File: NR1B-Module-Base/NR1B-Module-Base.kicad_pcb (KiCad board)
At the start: 2 copper layers, 70.5 x 134 mm, 3 parts, among them J1 Conn_02x04_Odd_Even, J2 Conn_02x04_Odd_Even, X1 NUCLEO144-ZIO

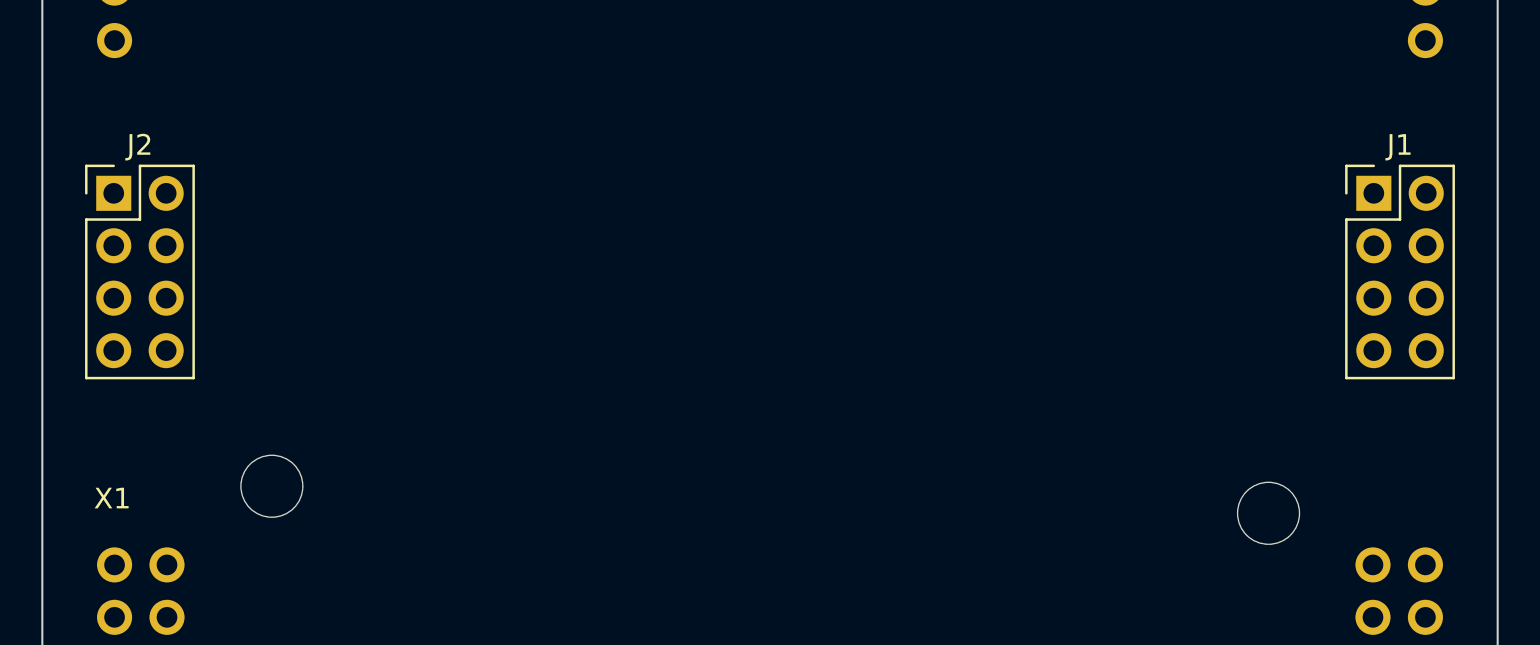
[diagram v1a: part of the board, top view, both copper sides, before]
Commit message: Updated template to match new interconnect spec
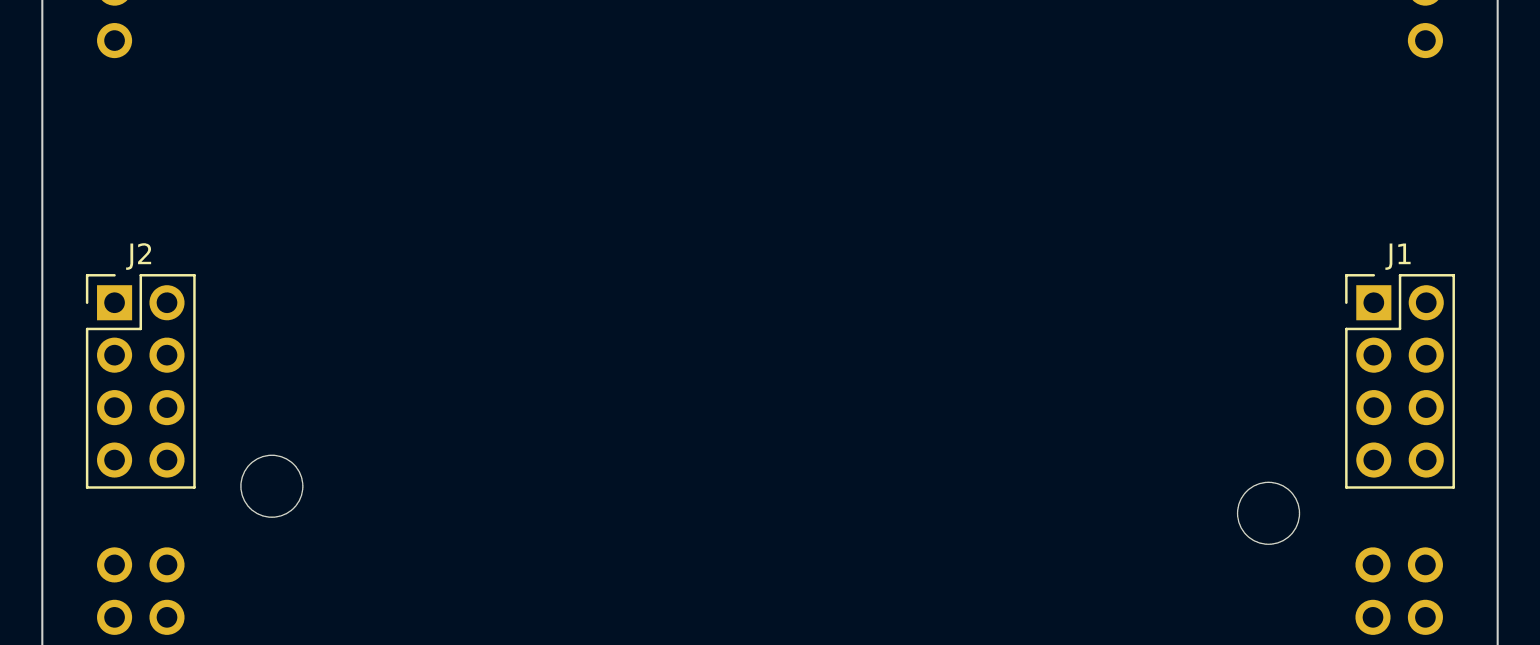
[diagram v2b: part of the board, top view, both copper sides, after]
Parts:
- moved J2 5.30 mm to (163.0, 99.3)
- moved J1 5.30 mm to (224.0, 99.3)
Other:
- board text added: "X1A"
- board text added: "X2A"
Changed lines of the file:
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@@
   (net 160 "unconnected-(J2-Pad8)")
   (footprint "Connector_PinHeader_2.54mm:PinHeader_2x04_P2.54mm_Vertical" (layer "F.Cu")
-    (at 162.96 94)
+    (at 163 99.3)
     (descr "Through hole straight pin header, 2x04, 2.54mm pitch, double rows")
     (tags "Through hole pin header THT 2x04 2.54mm double row")
@@
     (property "Sheetname" "")
     (attr through_hole)
-    (fp_text reference "X1" (at -0.1 -3.2) (layer "F.SilkS")
+    (fp_text reference "X1" (at -0.1 -3.2) (layer "F.SilkS") hide
       (effects (font (size 1 1) (thickness 0.15)))
     )
@@
       (effects (font (size 1 1) (thickness 0.15)))
     )
-    (fp_line (start 41.25 -32.24) (end 50.25 -32.24) (layer "F.CrtYd") (width 0.05))
-    (fp_line (start 67.25 102.16) (end 48.65 102.16) (layer "F.CrtYd") (width 0.05))
-    (fp_line (start 67.25 102.16) (end 67.25 -32.24) (layer "F.CrtYd") (width 0.05))
-    (fp_line (start -3.75 -32.24) (end -3.75 102.16) (layer "F.CrtYd") (width 0.05))
-    (fp_line (start 33.6 102.2) (end 48.65 102.16) (layer "F.CrtYd") (width 0.05))
-    (fp_line (start -3.75 102.16) (end 8.25 102.16) (layer "F.CrtYd") (width 0.05))
-    (fp_line (start 8.25 102.16) (end 17.25 102.16) (layer "F.CrtYd") (width 0.05))
-    (fp_line (start 17.25 102.16) (end 33.66 102.16) (layer "F.CrtYd") (width 0.05))
-    (fp_line (start 50.25 -32.24) (end 67.25 -32.24) (layer "F.CrtYd") (width 0.05))
-    (fp_line (start 41.25 -32.24) (end -3.75 -32.24) (layer "F.CrtYd") (width 0.05))
+    (fp_line (start 34.15 92.1) (end 48.15 92.1) (layer "F.Fab") (width 0.12))
     (fp_line (start 41.75 -27.74) (end 49.75 -27.74) (layer "F.Fab") (width 0.12))
+    (fp_line (start 16.75 97.66) (end 16.75 103.16) (layer "F.Fab") (width 0.12))
+    (fp_line (start 8.75 103.16) (end 16.75 103.16) (layer "F.Fab") (width 0.12))
+    (fp_line (start 8.75 103.16) (end 8.75 97.65) (layer "F.Fab") (width 0.12))
+    (fp_line (start 48.15 104.1) (end 48.15 92.1) (layer "F.Fab") (width 0.12))
+    (fp_line (start 49.75 -33.24) (end 49.75 -27.74) (layer "F.Fab") (width 0.12))
+    (fp_line (start 41.75 -33.24) (end 49.75 -33.24) (layer "F.Fab") (width 0.12))
+    (fp_line (start 66.45 -31.74) (end -2.95 -31.74) (layer "F.Fab") (width 0.1))
+    (fp_line (start 41.75 -27.74) (end 41.75 -33.24) (layer "F.Fab") (width 0.12))
+    (fp_line (start 66.75 101.36) (end 66.75 -31.44) (layer "F.Fab") (width 0.1))
+    (fp_line (start 66.45 101.66) (end -2.95 101.66) (layer "F.Fab") (width 0.1))
     (fp_line (start 8.75 97.66) (end 16.75 97.66) (layer "F.Fab") (width 0.12))
-    (fp_line (start 48.15 104.1) (end 48.15 92.1) (layer "F.Fab") (width 0.12))
-    (fp_line (start 66.45 -31.74) (end -2.95 -31.74) (layer "F.Fab") (width 0.1))
+    (fp_line (start -3.25 101.36) (end -3.25 -31.44) (layer "F.Fab") (width 0.1))
     (fp_line (start 34.15 104.1) (end 34.15 92.1) (layer "F.Fab") (width 0.12))
-    (fp_line (start 16.75 97.66) (end 16.75 103.16) (layer "F.Fab") (width 0.12))
-    (fp_line (start 66.45 101.66) (end -2.95 101.66) (layer "F.Fab") (width 0.1))
     (fp_line (start 34.15 104.1) (end 48.15 104.1) (layer "F.Fab") (width 0.12))
-    (fp_line (start 41.75 -33.24) (end 49.75 -33.24) (layer "F.Fab") (width 0.12))
-    (fp_line (start 8.75 103.16) (end 16.75 103.16) (layer "F.Fab") (width 0.12))
-    (fp_line (start 66.75 101.36) (end 66.75 -31.44) (layer "F.Fab") (width 0.1))
-    (fp_line (start 8.75 103.16) (end 8.75 97.65) (layer "F.Fab") (width 0.12))
-    (fp_line (start 49.75 -33.24) (end 49.75 -27.74) (layer "F.Fab") (width 0.12))
-    (fp_line (start 34.15 92.1) (end 48.15 92.1) (layer "F.Fab") (width 0.12))
-    (fp_line (start 41.75 -27.74) (end 41.75 -33.24) (layer "F.Fab") (width 0.12))
-    (fp_line (start -3.25 101.36) (end -3.25 -31.44) (layer "F.Fab") (width 0.1))
+    (fp_arc (start -2.95 101.66) (mid -3.162132 101.572132) (end -3.25 101.36) (layer "F.Fab") (width 0.1))
+    (fp_arc (start 66.75 101.36) (mid 66.662132 101.572132) (end 66.45 101.66) (layer "F.Fab") (width 0.1))
     (fp_arc (start 66.45 -31.74) (mid 66.662132 -31.652132) (end 66.75 -31.44) (layer "F.Fab") (width 0.1))
     (fp_arc (start -3.25 -31.44) (mid -3.162132 -31.652132) (end -2.95 -31.74) (layer "F.Fab") (width 0.1))
-    (fp_arc (start 66.75 101.36) (mid 66.662132 101.572132) (end 66.45 101.66) (layer "F.Fab") (width 0.1))
-    (fp_arc (start -2.95 101.66) (mid -3.162132 101.572132) (end -3.25 101.36) (layer "F.Fab") (width 0.1))
-    (pad "" np_thru_hole circle (at 8.89 72.39) (size 3 3) (drill 3) (layers *.Cu *.Mask))
-    (pad "" np_thru_hole circle (at 40.55 48.3) (size 3 3) (drill 3) (layers *.Cu *.Mask))
-    (pad "" np_thru_hole circle (at 7.62 -3.81) (size 3 3) (drill 3) (layers *.Cu *.Mask))
     (pad "" np_thru_hole circle (at 55.9 -2.5) (size 3 3) (drill 3) (layers *.Cu *.Mask))
     (pad "" np_thru_hole circle (at 54.6 72.4) (size 3 3) (drill 3) (layers *.Cu *.Mask))
+    (pad "" np_thru_hole circle (at 40.55 48.3) (size 3 3) (drill 3) (layers *.Cu *.Mask))
+    (pad "" np_thru_hole circle (at 8.89 72.39) (size 3 3) (drill 3) (layers *.Cu *.Mask))
+    (pad "" np_thru_hole circle (at 7.62 -3.81) (size 3 3) (drill 3) (layers *.Cu *.Mask))
     (pad "1" thru_hole circle (at 0 0) (size 1.7 1.7) (drill 1) (layers *.Cu *.Mask)
       (net 1 "unconnected-(X1-Pad1)") (pinfunction "PC10") (pintype "bidirectional"))
@@
   )
   (footprint "Connector_PinHeader_2.54mm:PinHeader_2x04_P2.54mm_Vertical" (layer "F.Cu")
-    (at 224 94)
+    (at 224 99.3)
     (descr "Through hole straight pin header, 2x04, 2.54mm pitch, double rows")
     (tags "Through hole pin header THT 2x04 2.54mm double row")
@@
   (gr_line (start 230 80) (end 230 214) (layer "Edge.Cuts") (width 0.1))
   (gr_line (start 159.5 214) (end 159.5 80) (layer "Edge.Cuts") (width 0.1))
+  (gr_text "X2A" (at 221.25 112.25) (layer "F.Fab")
+    (effects (font (size 1 1) (thickness 0.15)))
+  )
+  (gr_text "X1A" (at 168.5 112) (layer "F.Fab")
+    (effects (font (size 1 1) (thickness 0.15)))
+  )
+  (dimension (type aligned) (layer "F.Fab")
+    (pts (xy 163 112) (xy 163 99.3))
+    (height -7.75)
+    (gr_text "12.7000 mm" (at 154.1 105.65 90) (layer "F.Fab")
+      (effects (font (size 1 1) (thickness 0.15)))
+    )
+    (format (units 3) (units_format 1) (precision 4))
+    (style (thickness 0.1) (arrow_length 1.27) (text_position_mode 0) (extension_height 0.58642) (extension_offset 0.5) keep_text_aligned)
+  )
+  (dimension (type aligned) (layer "F.Fab")
+    (pts (xy 163 99.3) (xy 159.5 99.3))
+    (height 21.05)
+    (gr_text "3.5000 mm" (at 161.25 77.1) (layer "F.Fab")
+      (effects (font (size 1 1) (thickness 0.15)))
+    )
+    (format (units 3) (units_format 1) (precision 4))
+    (style (thickness 0.1) (arrow_length 1.27) (text_position_mode 0) (extension_height 0.58642) (extension_offset 0.5) keep_text_aligned)
+  )
+  (dimension (type aligned) (layer "F.Fab")
+    (pts (xy 159.5 80) (xy 230 80))
+    (height -6.75)
+    (gr_text "70.5000 mm" (at 194.75 72.1) (layer "F.Fab")
+      (effects (font (size 1 1) (thickness 0.15)))
+    )
+    (format (units 3) (units_format 1) (precision 4))
+    (style (thickness 0.1) (arrow_length 1.27) (text_position_mode 0) (extension_height 0.58642) (extension_offset 0.5) keep_text_aligned)
+  )
+  (dimension (type aligned) (layer "F.Fab")
+    (pts (xy 224 99.3) (xy 163 99.3))
+    (height 23.55)
+    (gr_text "61.0000 mm" (at 193.5 74.6) (layer "F.Fab")
+      (effects (font (size 1 1) (thickness 0.15)))
+    )
+    (format (units 3) (units_format 1) (precision 4))
+    (style (thickness 0.1) (arrow_length 1.27) (text_position_mode 0) (extension_height 0.58642) (extension_offset 0.5) keep_text_aligned)
+  )
+  (dimension (type aligned) (layer "F.Fab")
+    (pts (xy 159.5 80) (xy 159.5 214))
+    (height 7.249999)
+    (gr_text "134.0000 mm" (at 151.100001 147 90) (layer "F.Fab")
+      (effects (font (size 1 1) (thickness 0.15)))
+    )
+    (format (units 3) (units_format 1) (precision 4))
+    (style (thickness 0.1) (arrow_length 1.27) (text_position_mode 0) (extension_height 0.58642) (extension_offset 0.5) keep_text_aligned)
+  )
 )
